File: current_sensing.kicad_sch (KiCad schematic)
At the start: 22 parts, among them IC6 AD8030ARZ, IC7 AD8030ARZ

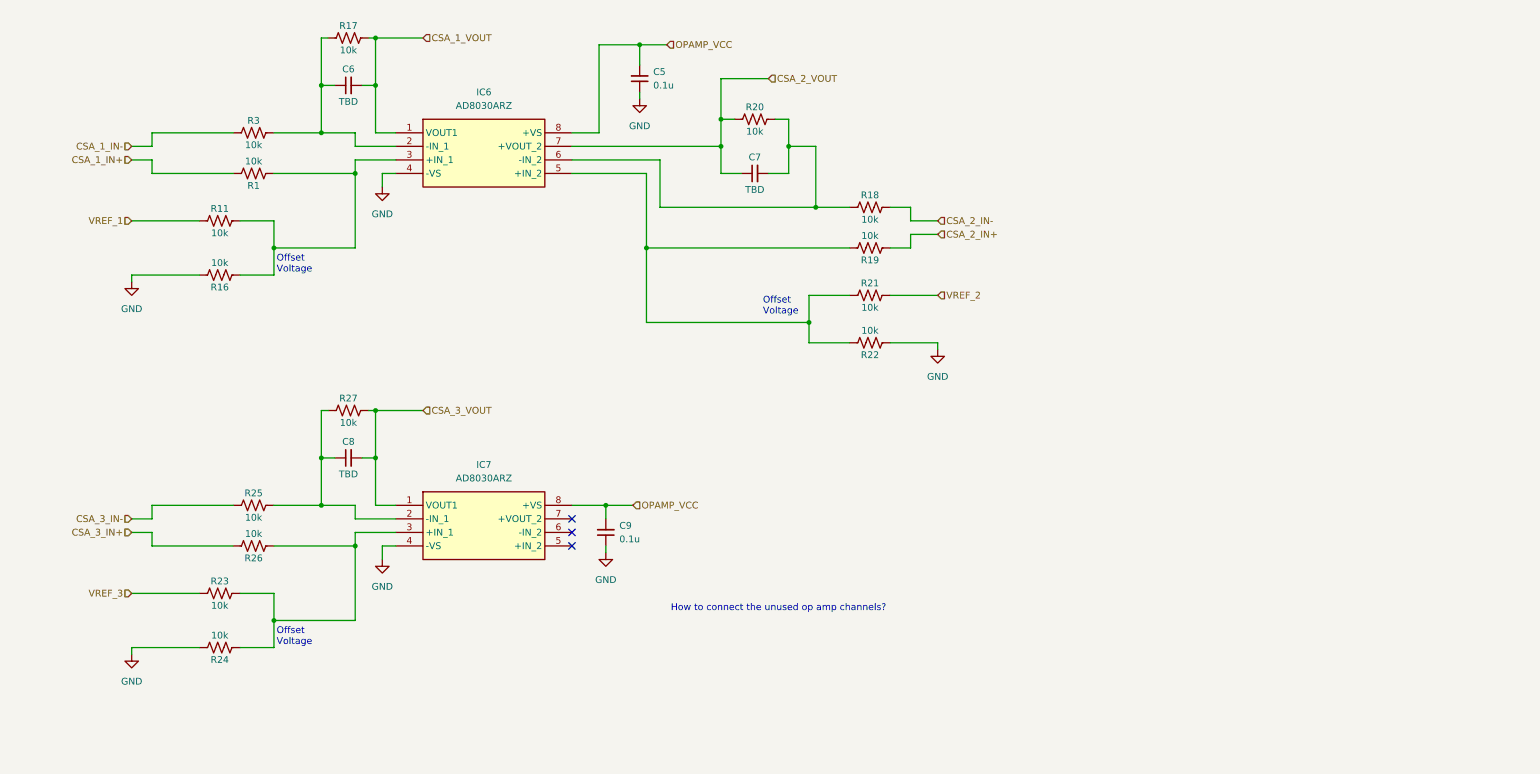
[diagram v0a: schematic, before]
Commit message: Add MCU stuff, cortex debug connector and docs
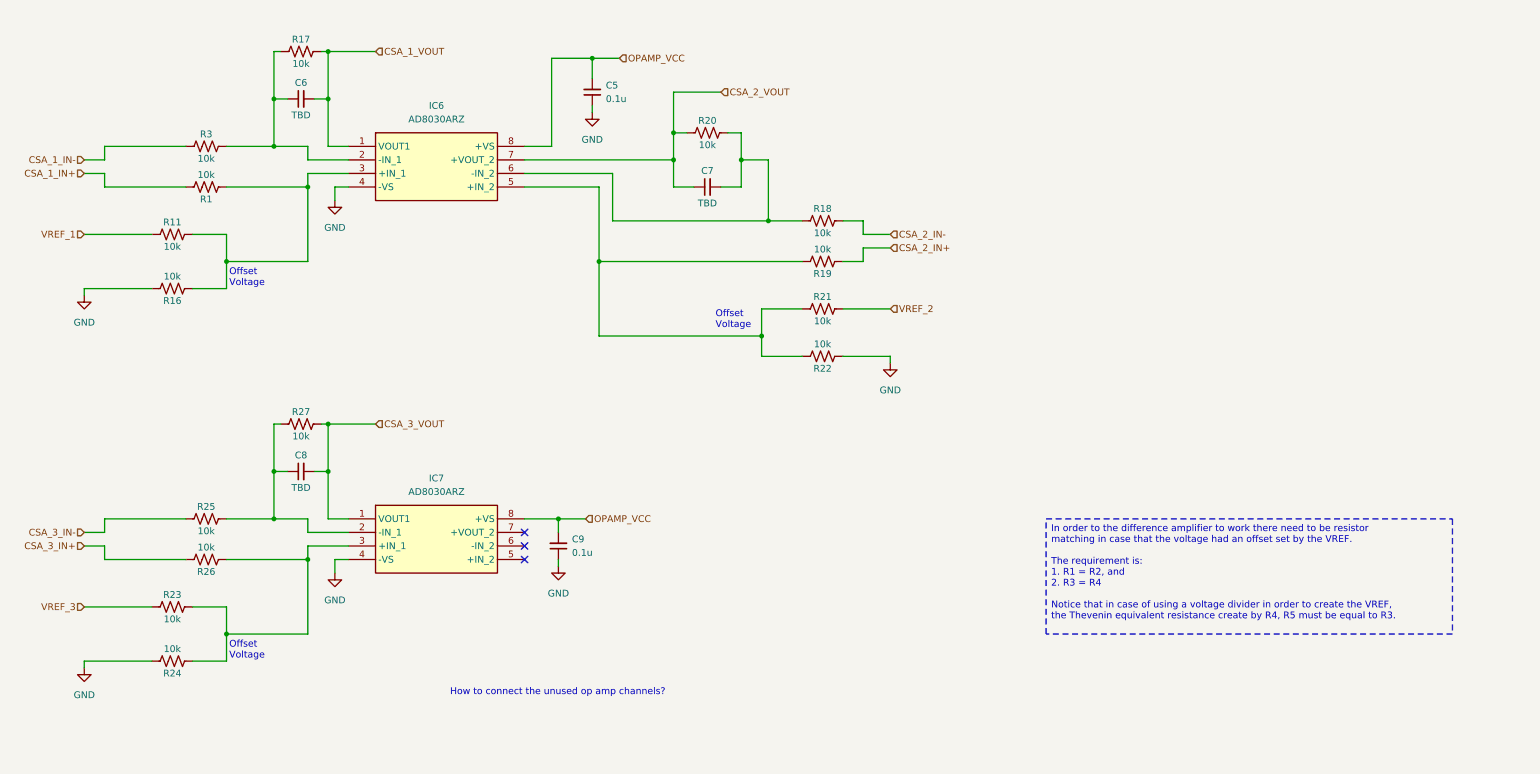
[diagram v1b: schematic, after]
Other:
- moved on the sheet: C5, C6, C7, C8, C9, IC6, IC7, R1, R11, R16, R17, R18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

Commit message: Connect unused op amp channel
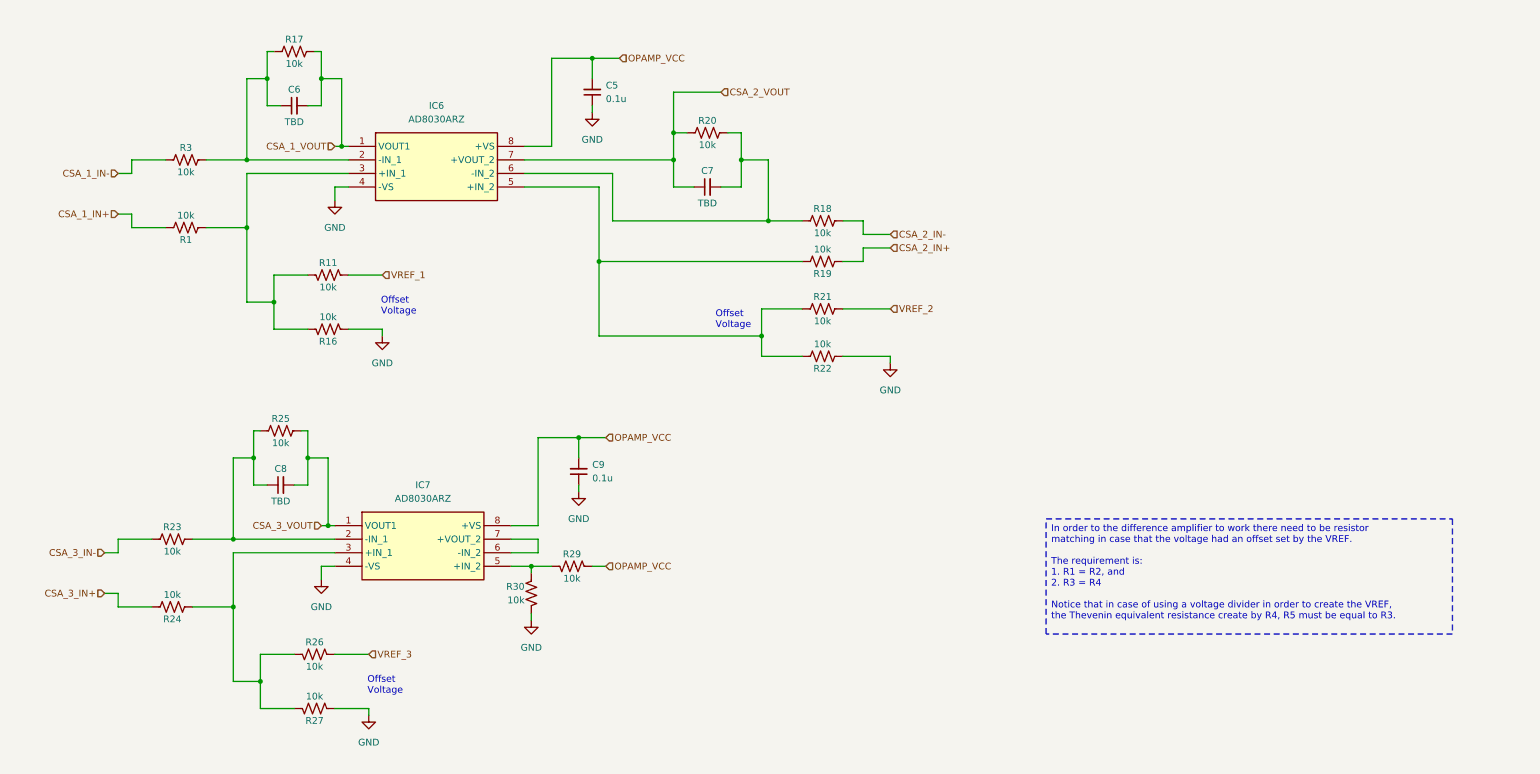
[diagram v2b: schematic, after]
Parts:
- added R29, R30: 10k, symbol Device:R_US
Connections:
- net CSA_3_IN+: now also R24.2; no longer R26.2
- net CSA_3_IN-: now also R23.1; no longer R25.1
- net CSA_3_VOUT: now also R25.2; no longer R27.2
- net GND: now also R27.2, R30.2; no longer R24.2
- net OPAMP_VCC: now also R29.1
- net VREF_3: now also R26.1; no longer R23.1
- net at IC7.3 (+IN_1), R24.1: now also R26.2, R27.1; no longer R23.2, R26.1
- net at C8.1, IC7.2 (-IN_1): now also R23.2, R25.1; no longer R25.2, R27.1
- net at IC7.5 (+IN_2): now also R29.2, R30.1
- net at IC7.6 (-IN_2): now also IC7.7 (+VOUT_2)
- no-connect marks 3 -> 0
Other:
- note removed: "How to connect the unused op amp channels?"
- moved on the sheet: C6, R1, R11, R16, R17, R3

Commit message: Add gitignore
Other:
- moved on the sheet: C5, C7, C8, C9, IC7, R11, R16, R18, R19, R20, R21, R22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

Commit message: Initial routing
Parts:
- C5, C6, C7, C8, C9: footprint (none) -> Capacitor_SMD:C_0603_1608Metric
- R1, R11, R16, R17, R18, R19, R20, R21, R22, R23, R24, R25, R26, R27, R29, R3, R30: footprint (none) -> Resistor_SMD:R_0603_1608Metric
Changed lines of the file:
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@@
 			)
 		)
-		(property "Footprint" ""
+		(property "Footprint" "Resistor_SMD:R_0603_1608Metric"
 			(at 71.374 79.756 90)
 			(effects
@@
 			)
 		)
-		(property "Footprint" ""
+		(property "Footprint" "Resistor_SMD:R_0603_1608Metric"
 			(at 120.396 125.984 90)
 			(effects
@@
 			)
 		)
-		(property "Footprint" ""
+		(property "Footprint" "Resistor_SMD:R_0603_1608Metric"
 			(at 152.654 58.674 90)
 			(effects
@@
 			)
 		)
-		(property "Footprint" ""
+		(property "Footprint" "Resistor_SMD:R_0603_1608Metric"
 			(at 136.144 73.914 90)
 			(effects
@@
 			)
 		)
-		(property "Footprint" ""
+		(property "Footprint" "Resistor_SMD:R_0603_1608Metric"
 			(at 65.024 26.924 90)
 			(effects
@@
 			)
 		)
-		(property "Footprint" ""
+		(property "Footprint" "Resistor_SMD:R_0603_1608Metric"
 			(at 44.704 47.244 90)
 			(effects
@@
 			)
 		)
-		(property "Footprint" ""
+		(property "Footprint" "Capacitor_SMD:C_0603_1608Metric"
 			(at 118.11 27.94 0)
 			(effects
@@
 			)
 		)
-		(property "Footprint" ""
+		(property "Footprint" "Capacitor_SMD:C_0603_1608Metric"
 			(at 120.65 109.22 0)
 			(effects
@@
 			)
 		)
-		(property "Footprint" ""
+		(property "Footprint" "Resistor_SMD:R_0603_1608Metric"
 			(at 44.196 61.976 90)
 			(effects
@@
 			)
 		)
-		(property "Footprint" ""
+		(property "Footprint" "Resistor_SMD:R_0603_1608Metric"
 			(at 72.136 142.494 90)
 			(effects
@@
 			)
 		)
-		(property "Footprint" ""
+		(property "Footprint" "Resistor_SMD:R_0603_1608Metric"
 			(at 70.866 70.104 90)
 			(effects
@@
 			)
 		)
-		(property "Footprint" ""
+		(property "Footprint" "Resistor_SMD:R_0603_1608Metric"
 			(at 66.294 100.584 90)
 			(effects
@@
 			)
 		)
-		(property "Footprint" ""
+		(property "Footprint" "Capacitor_SMD:C_0603_1608Metric"
 			(at 135.89 41.91 0)
 			(effects
@@
 			)
 		)
-		(property "Footprint" ""
+		(property "Footprint" "Resistor_SMD:R_0603_1608Metric"
 			(at 72.644 154.686 90)
 			(effects
@@
 			)
 		)
-		(property "Footprint" ""
+		(property "Footprint" "Capacitor_SMD:C_0603_1608Metric"
 			(at 64.77 38.1 0)
 			(effects
@@
 			)
 		)
-		(property "Footprint" ""
+		(property "Footprint" "Resistor_SMD:R_0603_1608Metric"
 			(at 136.144 32.004 90)
 			(effects
@@
 			)
 		)
-		(property "Footprint" ""
+		(property "Footprint" "Resistor_SMD:R_0603_1608Metric"
 			(at 45.974 120.904 90)
 			(effects
@@
 			)
 		)
-		(property "Footprint" ""
+		(property "Footprint" "Capacitor_SMD:C_0603_1608Metric"
 			(at 66.04 111.76 0)
 			(effects
@@
 			)
 		)
-		(property "Footprint" ""
+		(property "Footprint" "Resistor_SMD:R_0603_1608Metric"
 			(at 45.466 135.636 90)
 			(effects
@@
 			)
 		)
-		(property "Footprint" ""
+		(property "Footprint" "Resistor_SMD:R_0603_1608Metric"
 			(at 135.636 83.566 90)
 			(effects
@@
 			)
 		)
-		(property "Footprint" ""
+		(property "Footprint" "Resistor_SMD:R_0603_1608Metric"
 			(at 139.446 68.326 90)
 			(effects
@@
 			)
 		)
-		(property "Footprint" ""
+		(property "Footprint" "Resistor_SMD:R_0603_1608Metric"
 			(at 112.014 132.334 90)
 			(effects
